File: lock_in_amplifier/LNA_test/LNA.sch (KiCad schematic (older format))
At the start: 47 parts, among them J17 RF_Shield_One_Piece, J38 RF_Shield_One_Piece, U6 lmp7721, U7 LM833, U8 AD8429

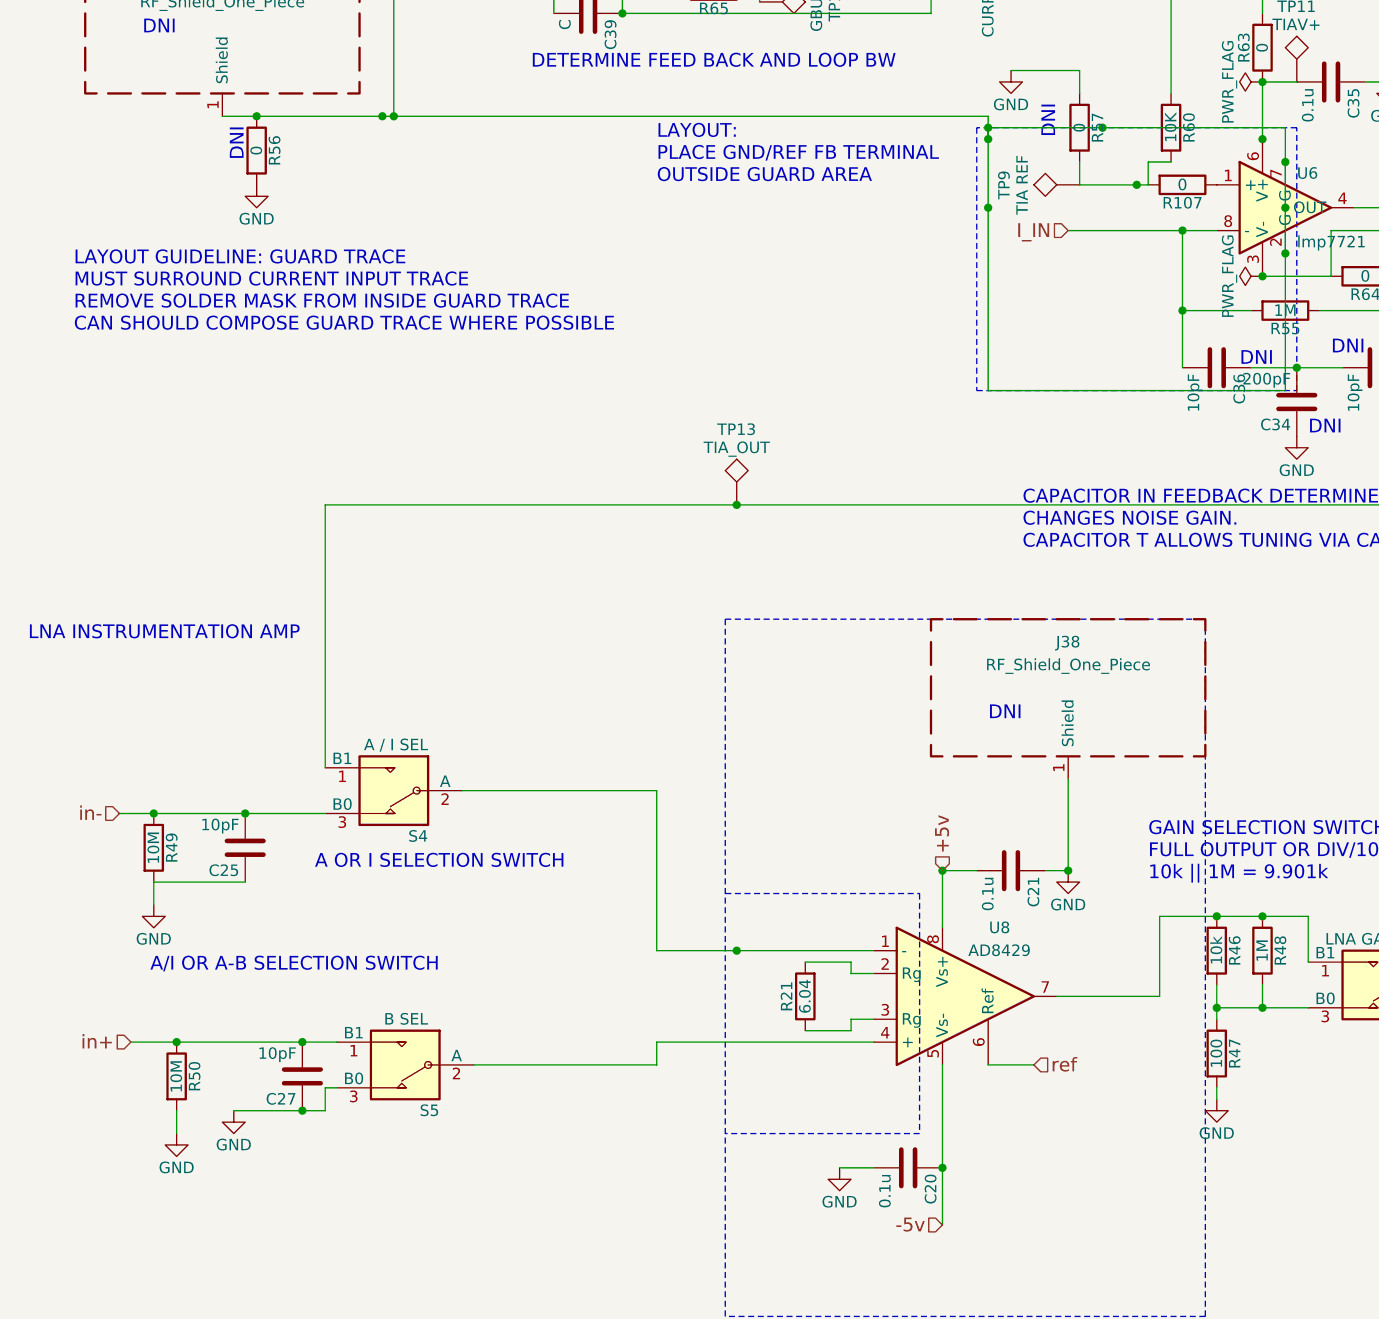
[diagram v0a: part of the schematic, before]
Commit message: started LNA test board.
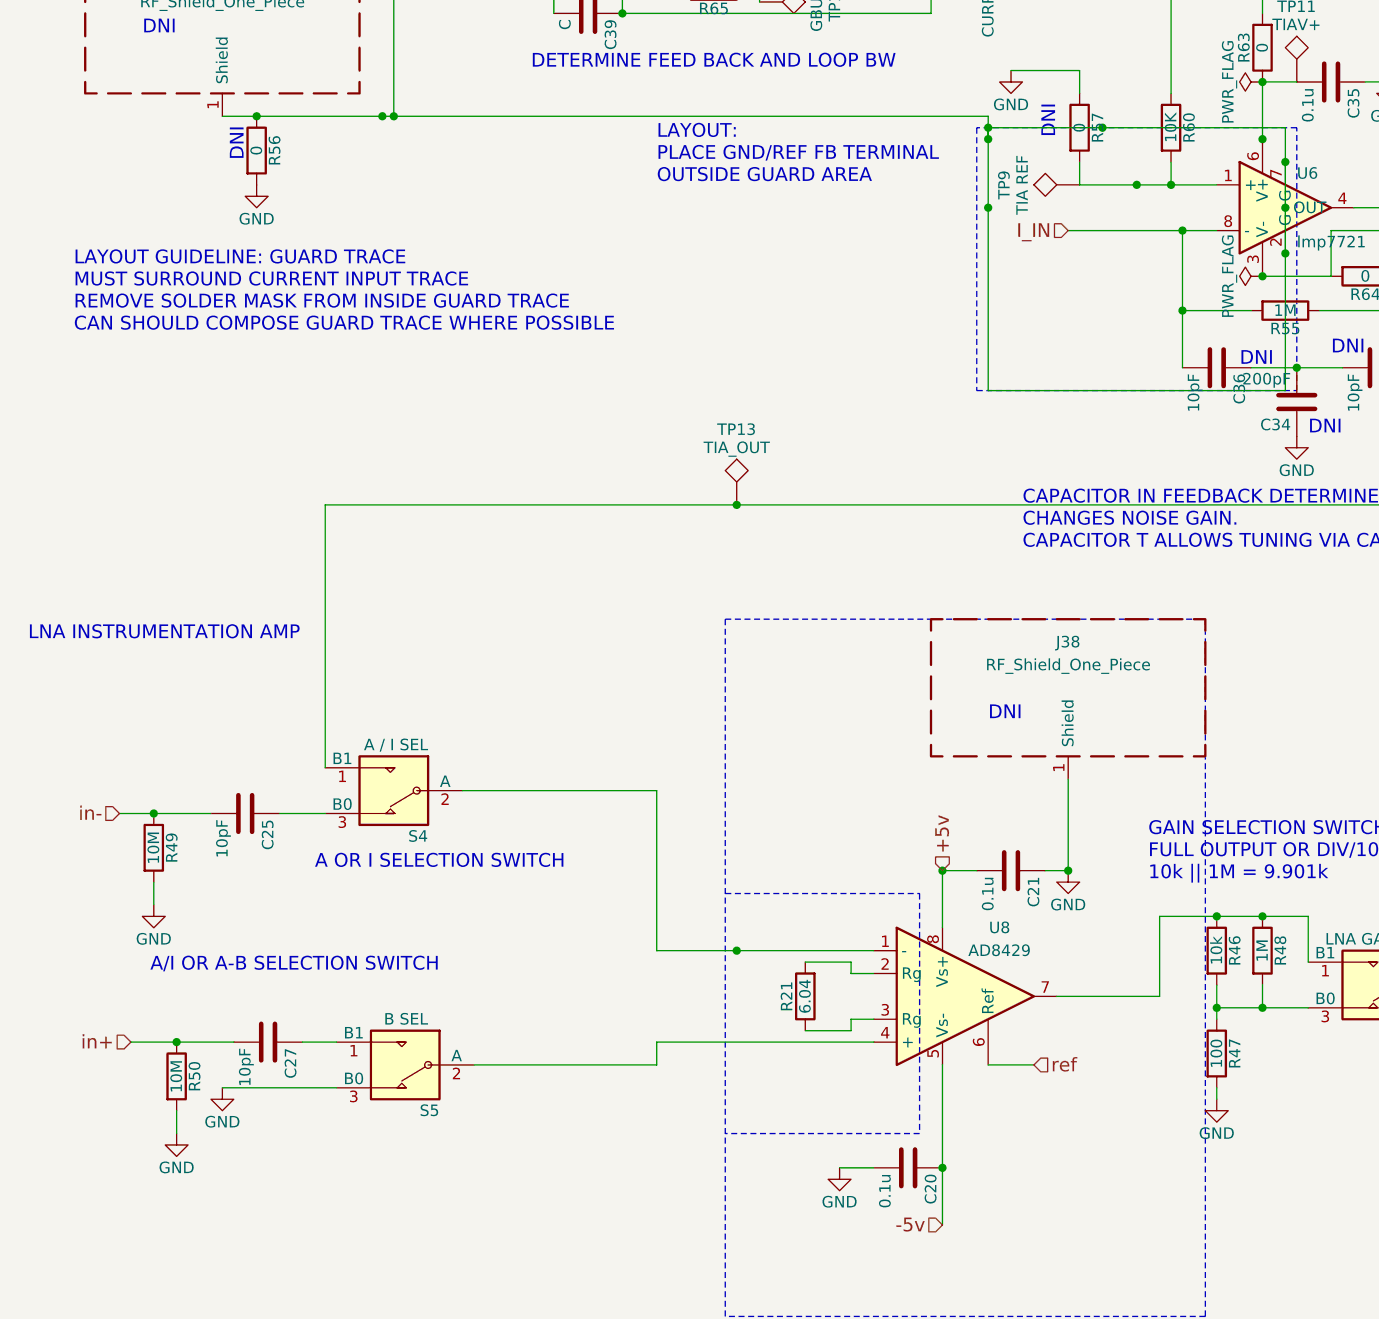
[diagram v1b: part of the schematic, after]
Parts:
- removed R107: 0, Resistors_SMD:R_0805, symbol R
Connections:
- net GND: no longer C25.1, C27.1
- net in+: no longer S5.1 (B1)
- net in-: no longer S4.3 (B0)
- net at R57.2, R60.2, TP9.1: now also U6.1 (+)
- new net: C25.1, S4.3 (B0)
- new net: C27.1, S5.1 (B1)
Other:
- moved on the sheet: C25, C27
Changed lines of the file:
@@
 $EndComp
 $Comp
-L GND #PWR042
+L GND #PWR073
 U 1 1 5A1C75B0
 P 4100 7200
-F 0 "#PWR042" H 4100 6950 50  0001 C CNN
+F 0 "#PWR073" H 4100 6950 50  0001 C CNN
 F 1 "GND" H 4100 7050 50  0000 C CNN
 F 2 "" H 4100 7200 50  0001 C CNN
@@
 $EndComp
 $Comp
-L GND #PWR043
+L GND #PWR074
 U 1 1 5A1C75B6
 P 5100 5900
-F 0 "#PWR043" H 5100 5650 50  0001 C CNN
+F 0 "#PWR074" H 5100 5650 50  0001 C CNN
 F 1 "GND" H 5100 5750 50  0000 C CNN
 F 2 "" H 5100 5900 50  0001 C CNN
@@
 TRANSIMPEDANCE AMPLIFIER
 $Comp
-L GND #PWR044
+L GND #PWR075
 U 1 1 5A1F5BDB
-P 1450 6950
-F 0 "#PWR044" H 1450 6700 50  0001 C CNN
-F 1 "GND" H 1450 6800 50  0000 C CNN
-F 2 "" H 1450 6950 50  0001 C CNN
-F 3 "" H 1450 6950 50  0001 C CNN
-	1    1450 6950
+P 1400 6850
+F 0 "#PWR075" H 1400 6600 50  0001 C CNN
+F 1 "GND" H 1400 6700 50  0000 C CNN
+F 2 "" H 1400 6850 50  0001 C CNN
+F 3 "" H 1400 6850 50  0001 C CNN
+	1    1400 6850
 	1    0    0    -1
 $EndComp
@@
 $EndComp
 $Comp
-L GND #PWR045
+L GND #PWR076
 U 1 1 5A276A01
 P 5750 6900
-F 0 "#PWR045" H 5750 6650 50  0001 C CNN
+F 0 "#PWR076" H 5750 6650 50  0001 C CNN
 F 1 "GND" H 5750 6750 50  0000 C CNN
 F 2 "" H 5750 6900 50  0001 C CNN
@@
 $EndComp
 $Comp
-L GND #PWR046
+L GND #PWR077
 U 1 1 5A277FAE
 P 1100 6050
-F 0 "#PWR046" H 1100 5800 50  0001 C CNN
+F 0 "#PWR077" H 1100 5800 50  0001 C CNN
 F 1 "GND" H 1100 5900 50  0000 C CNN
 F 2 "" H 1100 6050 50  0001 C CNN
@@
 $EndComp
 $Comp
-L GND #PWR047
+L GND #PWR078
 U 1 1 5A277FE0
 P 1200 7050
-F 0 "#PWR047" H 1200 6800 50  0001 C CNN
+F 0 "#PWR078" H 1200 6800 50  0001 C CNN
 F 1 "GND" H 1200 6900 50  0000 C CNN
 F 2 "" H 1200 7050 50  0001 C CNN
@@
 L C C25
 U 1 1 5A27810B
-P 1500 5800
-F 0 "C25" H 1525 5900 50  0000 L CNN
-F 1 "10pF" H 1525 5700 50  0000 L CNN
-F 2 "Capacitors_SMD:C_0805" H 1538 5650 50  0001 C CNN
-F 3 "" H 1500 5800 50  0001 C CNN
-	1    1500 5800
-	-1   0    0    1
+P 1500 5650
+F 0 "C25" H 1525 5750 50  0000 L CNN
+F 1 "10pF" H 1525 5550 50  0000 L CNN
+F 2 "Capacitors_SMD:C_0805" H 1538 5500 50  0001 C CNN
+F 3 "" H 1500 5650 50  0001 C CNN
+	1    1500 5650
+	0    1    1    0
 $EndComp
 $Comp
 L C C27
 U 1 1 5A278176
-P 1750 6800
-F 0 "C27" H 1775 6900 50  0000 L CNN
-F 1 "10pF" H 1775 6700 50  0000 L CNN
-F 2 "Capacitors_SMD:C_0805" H 1788 6650 50  0001 C CNN
-F 3 "" H 1750 6800 50  0001 C CNN
-	1    1750 6800
-	-1   0    0    1
+P 1600 6650
+F 0 "C27" H 1625 6750 50  0000 L CNN
+F 1 "10pF" H 1625 6550 50  0000 L CNN
+F 2 "Capacitors_SMD:C_0805" H 1638 6500 50  0001 C CNN
+F 3 "" H 1600 6650 50  0001 C CNN
+	1    1600 6650
+	0    1    1    0
 $EndComp
 $Comp
@@
 $EndComp
 $Comp
-L GND #PWR048
+L GND #PWR079
 U 1 1 5A21D13B
 P 6850 3300
-F 0 "#PWR048" H 6850 3050 50  0001 C CNN
+F 0 "#PWR079" H 6850 3050 50  0001 C CNN
 F 1 "GND" H 6850 3150 50  0000 C CNN
 F 2 "" H 6850 3300 50  0001 C CNN
@@
 $EndComp
 $Comp
-L GND #PWR049
+L GND #PWR080
 U 1 1 5A21D39E
 P 6500 2450
-F 0 "#PWR049" H 6500 2200 50  0001 C CNN
+F 0 "#PWR080" H 6500 2200 50  0001 C CNN
 F 1 "GND" H 6500 2300 50  0000 C CNN
 F 2 "" H 6500 2450 50  0001 C CNN
@@
 GUARD DRIVER
 $Comp
-L GND #PWR050
+L GND #PWR081
 U 1 1 5A220C69
 P 4200 1100
-F 0 "#PWR050" H 4200 850 50  0001 C CNN
+F 0 "#PWR081" H 4200 850 50  0001 C CNN
 F 1 "GND" H 4200 950 50  0000 C CNN
 F 2 "" H 4200 1100 50  0001 C CNN
@@
 +5v
 $Comp
-L GND #PWR051
+L GND #PWR082
 U 1 1 5A220E76
 P 4200 1800
-F 0 "#PWR051" H 4200 1550 50  0001 C CNN
+F 0 "#PWR082" H 4200 1550 50  0001 C CNN
 F 1 "GND" H 4200 1650 50  0000 C CNN
 F 2 "" H 4200 1800 50  0001 C CNN
@@
 $EndComp
 $Comp
-L GND #PWR052
+L GND #PWR083
 U 1 1 5A221F33
 P 1550 2900
-F 0 "#PWR052" H 1550 2650 50  0001 C CNN
+F 0 "#PWR083" H 1550 2650 50  0001 C CNN
 F 1 "GND" H 1550 2750 50  0000 C CNN
 F 2 "" H 1550 2900 50  0001 C CNN
@@
 DNI
 $Comp
-L GND #PWR053
+L GND #PWR084
 U 1 1 5A2235D5
 P 4850 2400
-F 0 "#PWR053" H 4850 2150 50  0001 C CNN
+F 0 "#PWR084" H 4850 2150 50  0001 C CNN
 F 1 "GND" H 4850 2250 50  0000 C CNN
 F 2 "" H 4850 2400 50  0001 C CNN
@@
 DNI
 $Comp
-L GND #PWR054
+L GND #PWR085
 U 1 1 5A2424BB
 P 6100 4000
-F 0 "#PWR054" H 6100 3750 50  0001 C CNN
+F 0 "#PWR085" H 6100 3750 50  0001 C CNN
 F 1 "GND" H 6100 3850 50  0000 C CNN
 F 2 "" H 6100 4000 50  0001 C CNN
@@
 Wire Wire Line
 	3300 6250 4250 6250
+Wire Wire Line
+	1900 6850 1400 6850
 Connection ~ 3650 6250
 Connection ~ 5100 5900
@@
 	1200 6950 1200 7050
 Wire Wire Line
-	1000 6650 1900 6650
+	1000 6650 1450 6650
 Connection ~ 1200 6650
 Wire Wire Line
-	950  5650 1850 5650
+	1750 6650 1900 6650
+Wire Wire Line
+	950  5650 1350 5650
 Connection ~ 1100 5650
+Wire Wire Line
+	1650 5650 1850 5650
 Wire Wire Line
 	3300 6750 3300 6650
@@
 Connection ~ 6050 2800
 Wire Wire Line
-	5150 2900 5450 2900
+	5550 2900 5550 2800
+Wire Wire Line
+	5150 2900 5750 2900
 Connection ~ 4750 2650
 Connection ~ 1550 2600
@@
 Wire Wire Line
 	5150 2800 5150 2900
+Connection ~ 5550 2900
 Wire Wire Line
 	4850 2400 5150 2400
@@
 Connection ~ 3400 2050
 $Comp
-L PWR_FLAG #FLG055
+L PWR_FLAG #FLG086
 U 1 1 5A2D348D
 P 3650 1100
-F 0 "#FLG055" H 3650 1175 50  0001 C CNN
+F 0 "#FLG086" H 3650 1175 50  0001 C CNN
 F 1 "PWR_FLAG" H 3650 1250 50  0000 C CNN
 F 2 "" H 3650 1100 50  0001 C CNN
@@
 $EndComp
 $Comp
-L PWR_FLAG #FLG056
+L PWR_FLAG #FLG087
 U 1 1 5A2D35B5
 P 3650 1800
-F 0 "#FLG056" H 3650 1875 50  0001 C CNN
+F 0 "#FLG087" H 3650 1875 50  0001 C CNN
 F 1 "PWR_FLAG" H 3650 1950 50  0000 C CNN
 F 2 "" H 3650 1800 50  0001 C CNN
@@
 $EndComp
 $Comp
-L PWR_FLAG #FLG057
+L PWR_FLAG #FLG088
 U 1 1 5A2D36AF
 P 5950 2450
-F 0 "#FLG057" H 5950 2525 50  0001 C CNN
+F 0 "#FLG088" H 5950 2525 50  0001 C CNN
 F 1 "PWR_FLAG" H 5950 2600 50  0000 C CNN
 F 2 "" H 5950 2450 50  0001 C CNN
@@
 $EndComp
 $Comp
-L PWR_FLAG #FLG058
+L PWR_FLAG #FLG089
 U 1 1 5A2D374D
 P 5950 3300
-F 0 "#FLG058" H 5950 3375 50  0001 C CNN
+F 0 "#FLG089" H 5950 3375 50  0001 C CNN
 F 1 "PWR_FLAG" H 5950 3450 50  0000 C CNN
 F 2 "" H 5950 3300 50  0001 C CNN
@@
 	0    -1   -1   0
 $EndComp
-$Comp
-L R R107
-U 1 1 5A3351D4
-P 5600 2900
-F 0 "R107" V 5680 2900 50  0000 C CNN
-F 1 "0" V 5600 2900 50  0000 C CNN
-F 2 "Resistors_SMD:R_0805" V 5530 2900 50  0001 C CNN
-F 3 "" H 5600 2900 50  0001 C CNN
-	1    5600 2900
-	0    1    1    0
-$EndComp
-Wire Wire Line
-	5550 2800 5450 2800
-Wire Wire Line
-	5450 2800 5450 2900
-Connection ~ 1750 6650
-Wire Wire Line
-	1900 6850 1850 6850
-Wire Wire Line
-	1850 6850 1850 6950
-Wire Wire Line
-	1850 6950 1450 6950
-Connection ~ 1750 6950
-Connection ~ 1500 5650
-Wire Wire Line
-	1500 5950 1100 5950
 $EndSCHEMATC
